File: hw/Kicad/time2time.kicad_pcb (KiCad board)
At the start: 2 copper layers, 50 x 70 mm, 97 parts, among them J201 USB_B_Micro, J202 LIPO 1S, J301 Conn_display, J302 Conn_expansion, J303 Conn_E3Z-D62, Q301 TSM2312CX, SW1 SW_SPDT, SW301 SW_Push, SW302 SW_Push, SW303 SW_Push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

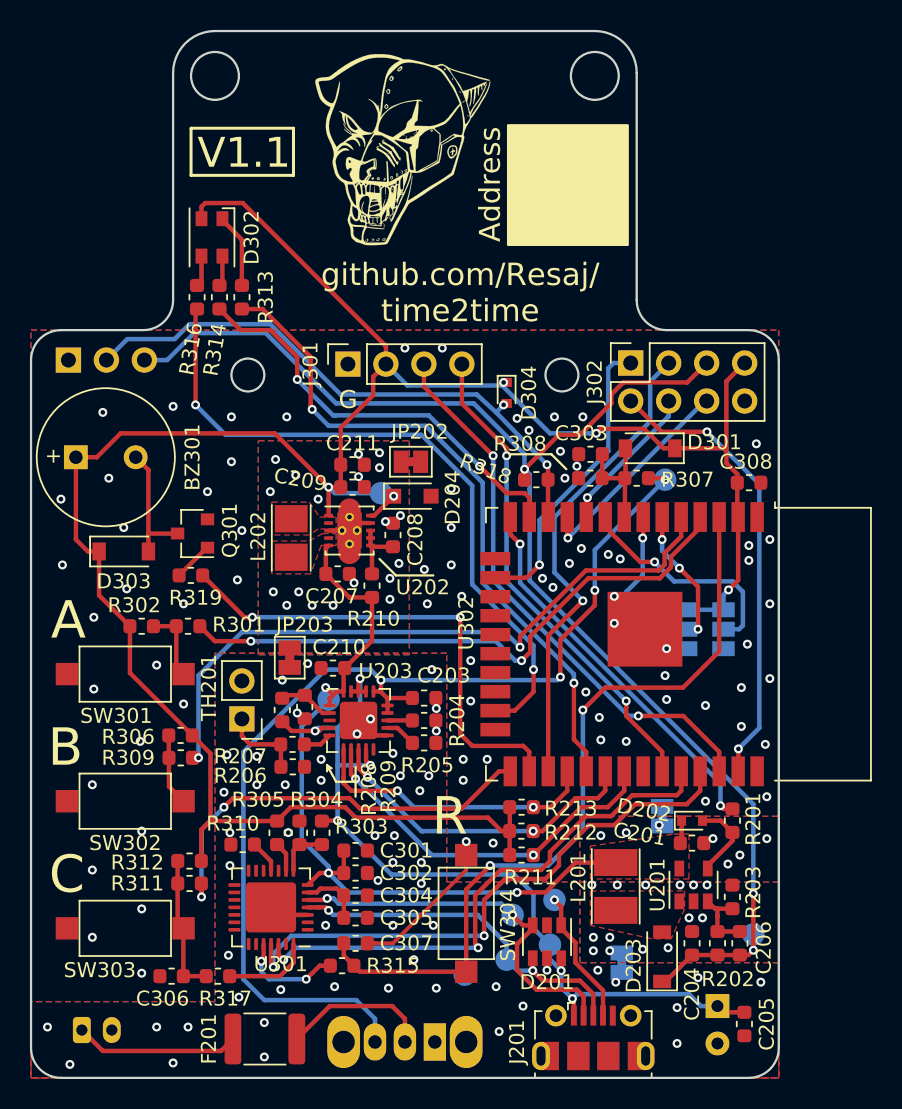
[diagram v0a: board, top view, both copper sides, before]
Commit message: hw. PCB modified to compliant with the clearance of 6mil between tracks and vias
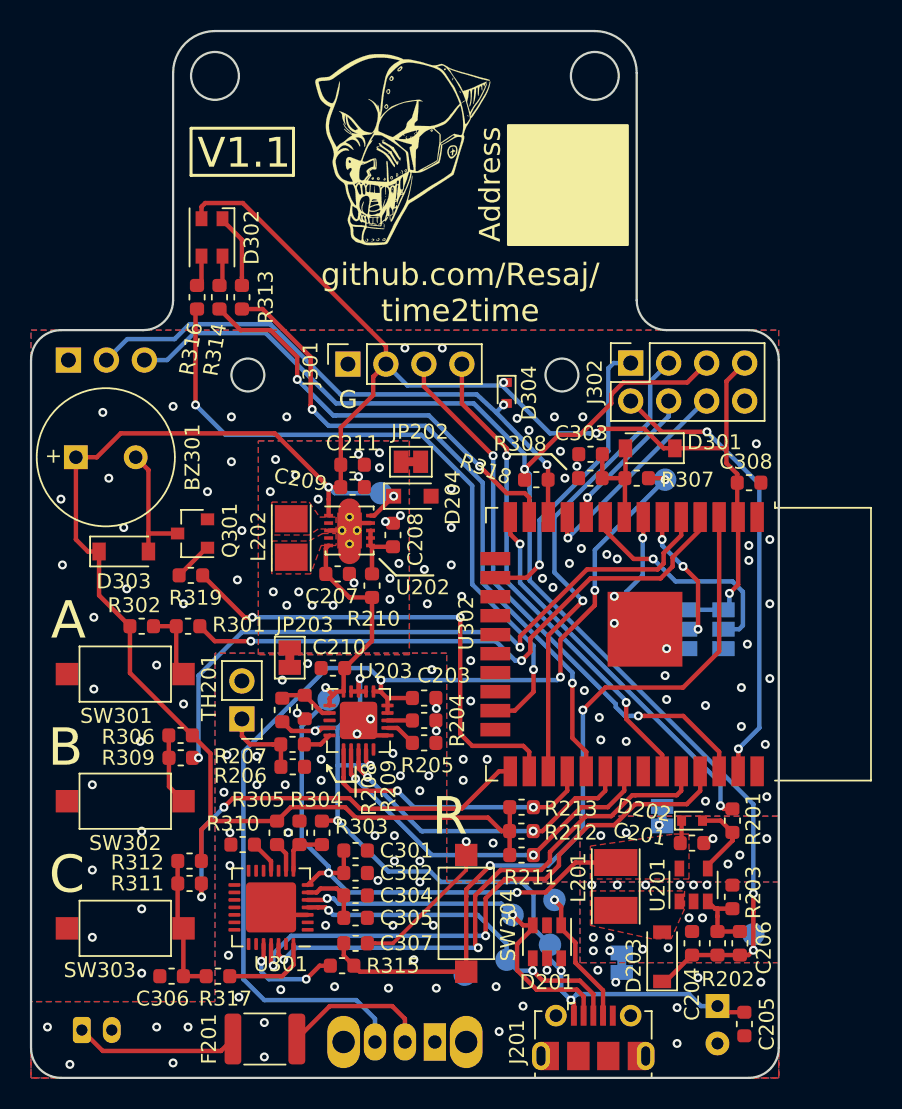
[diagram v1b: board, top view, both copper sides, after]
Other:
- net class Default: clearance 0.12 -> 0.155
- net class GND: clearance 0.12 -> 0.155
- net class Power: clearance 0.12 -> 0.155
- net class Signal: clearance 0.12 -> 0.155
- rule trace_clearance: 0.12 -> 0.155
